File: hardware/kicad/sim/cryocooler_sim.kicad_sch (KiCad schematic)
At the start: 17 parts, among them U1 OPA1656ID, U2 AD633JRZ-R7, U3 OPA188ID

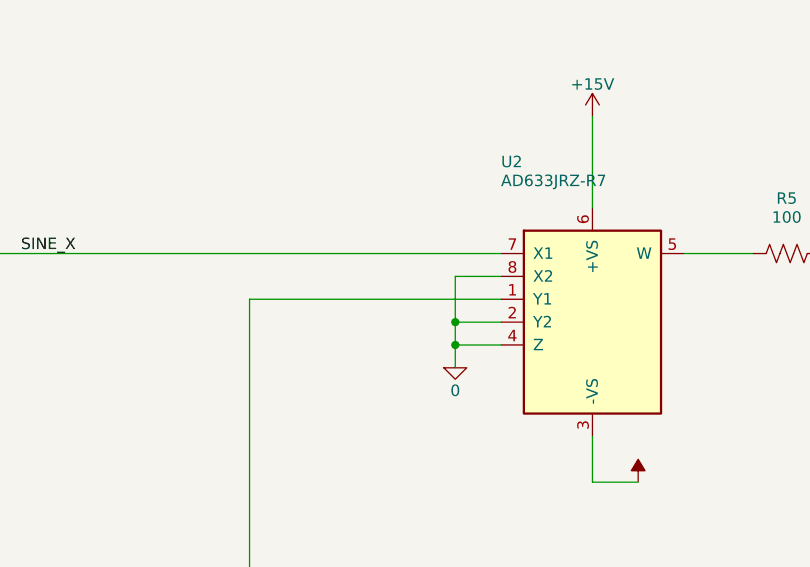
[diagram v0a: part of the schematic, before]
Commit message: Put supply pins on top and grounds on the bottom of IC symbols; flake8-clean Python
Schematic: re-laid out pins on U2, U3, U6, U7, U11, U14, U17-U20, U22-U24
and PS1 (supply on top, ground/strap pins on the bottom edge) via custom
`cryocooler:` symbols (make_lib.from_stock) and a gnd_bus helper; U18/U2
use mirroring instead of a 180 degree rotation. Nets are unchanged (ERC 0,
117/117 datasheet rules, PCB nets still match). Text placement now shows
every power-symbol name, avoids wires, and uses a realistic character width.

Python: black -l 79 -S plus manual wrapping so hardware/kicad and scripts/
pass flake8; add .flake8.

Co-Authored-By: Claude Sonnet 5.5 <noreply@anthropic.com>
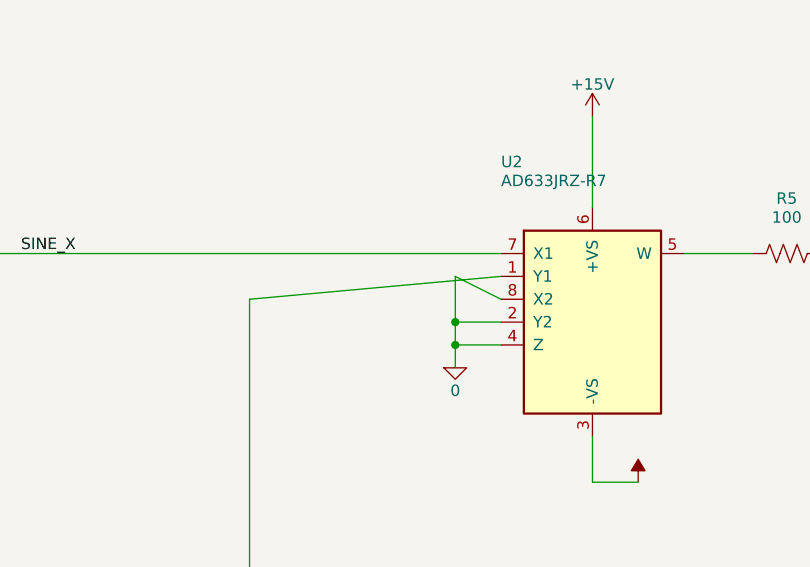
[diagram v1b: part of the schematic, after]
